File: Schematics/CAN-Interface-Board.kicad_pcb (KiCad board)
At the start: 4 copper layers, 50 x 100 mm, 71 parts, among them CN1 Limit Switch Connector 1, CN2 Limit Switch Connector 2, J1 Microsemi_FlashPro-JTAG-10, J2 USB_C_Receptacle, J3 Micro_SD_Card, J4 Screw_Terminal_01x02, J5 Screw_Terminal_01x02, J6 Conn_01x05_Pin, J7 Conn_01x04_Pin, U1 SN65HVD230, U2 LDL1117-3.3, U3 STM32F405RGT6, U5 LSM6DS3TR-C, U7 Bosch BMP388, Y1 8mhz

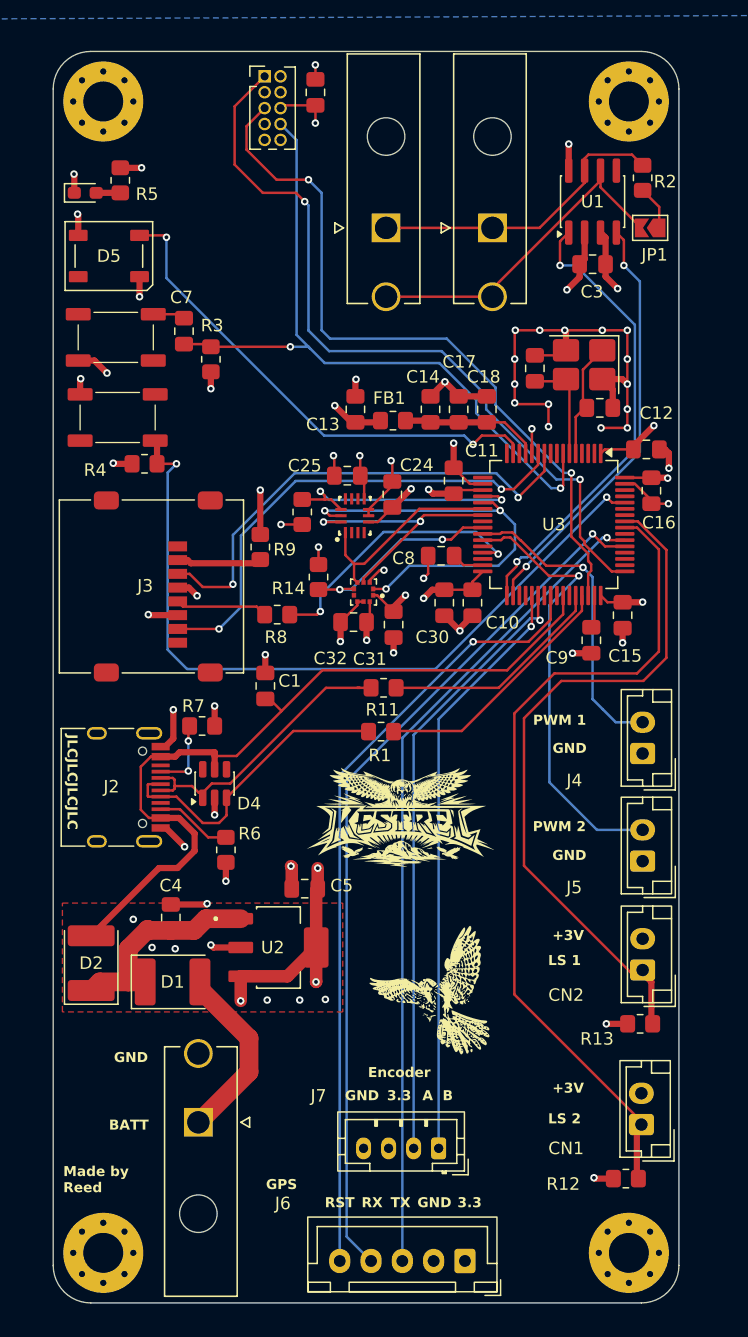
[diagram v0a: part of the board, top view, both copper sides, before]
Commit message: THIS is V2 look back for pin assignments final jlpcb cart for v1
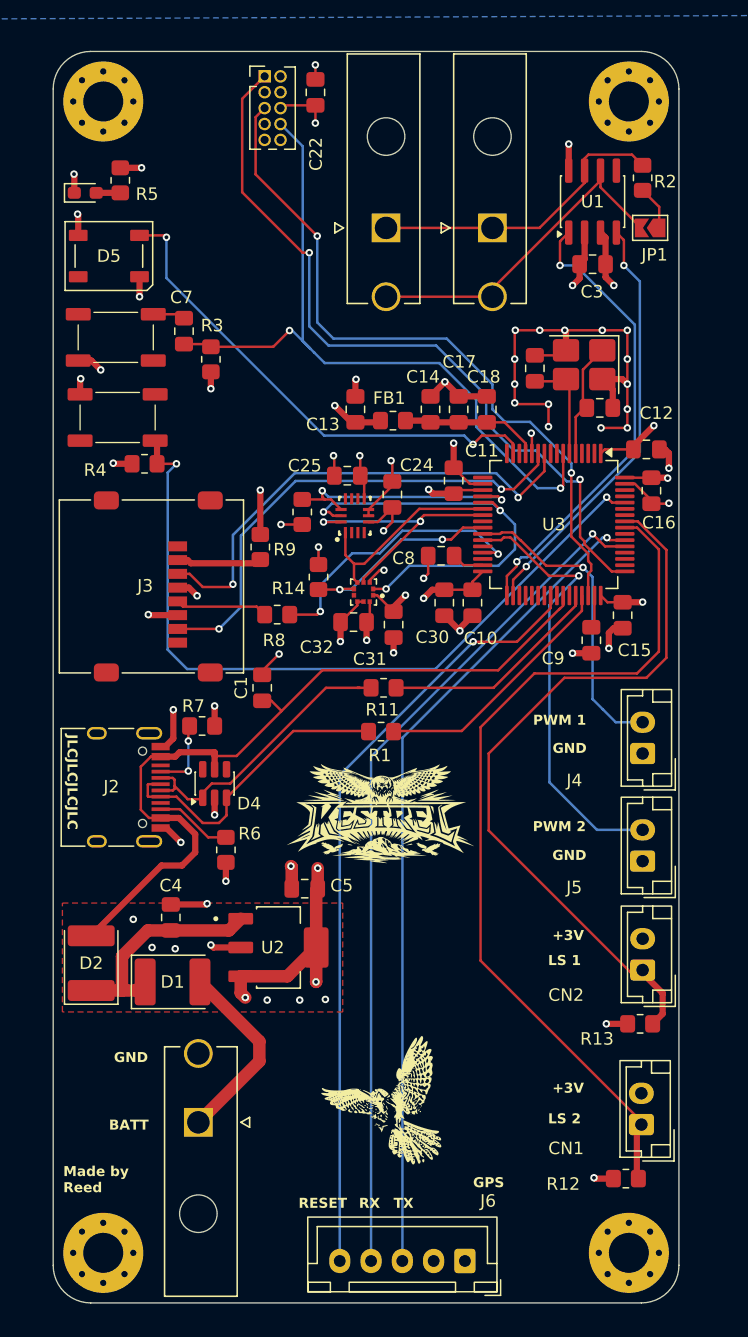
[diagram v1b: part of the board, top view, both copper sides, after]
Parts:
- removed J7: Conn_01x04_Pin, Connector_JST:JST_PH_B4B-PH-K_1x04_P2.00mm_Vertical
- moved G*** 9.61 mm to (136.3, 113.8)
- moved G*** 1.63 mm to (136.4, 92.0)
- moved C1 0.29 mm to (126.7, 80.8), turned to 90 degrees
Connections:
- C1 pad 1: GND -> /USB5V
- C1 pad 2: /USB5V -> GND
- U3 pad 37: /MCU/Encoder-B -> /MCU/CurrentCheck
- U3 pad 38: /MCU/Encoder-A -> unconnected-(U3-PC7-Pad38)
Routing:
- net /MCU/Encoder-A: track 49.1 -> 0.00 mm, vias 1 -> 0
- net /MCU/Encoder-B: track 47.3 -> 0.00 mm, vias 1 -> 0
- net /MCU/LimitSwitchCAS: track 66.6 -> 69.8 mm
- net /MCU/LimitSwitchRoll: track 55.5 -> 58.5 mm
- net /MCU/NRST: track 57.7 -> 59.4 mm
- net /GPS1_RX: track 70.0 -> 68.4 mm
- net /MCU/SWDIO: track 58.4 -> 56.9 mm
- net /MCU/SWCLK: track 62.0 -> 60.8 mm
- net Net-(D1-K): track 17.3 -> 18.1 mm
- net /USB Type C/D-: track 22.7 -> 23.4 mm
- net +BATT: track 15.0 -> 15.7 mm
- net /Barometer/Baraometer-SCK: track 33.5 -> 34.2 mm
- net /FlashSD/SDCLK: track 22.2 -> 22.7 mm
- net /RESET1: track 62.7 -> 62.2 mm
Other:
- board text added: "RESET"
- board text removed: "3.3"
- board text removed: "A"
- board text removed: "B"
- board text removed: "Encoder"
- board text removed: "RST"
